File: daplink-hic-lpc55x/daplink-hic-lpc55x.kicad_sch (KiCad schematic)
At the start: 27 parts, among them J1 Conn_01x12_Socket, J2 Conn_01x12_Socket, SW2 SW_Push, U1 LPC55x16JEV98E, Y1 ABM8-16.000MHZ-B2-T

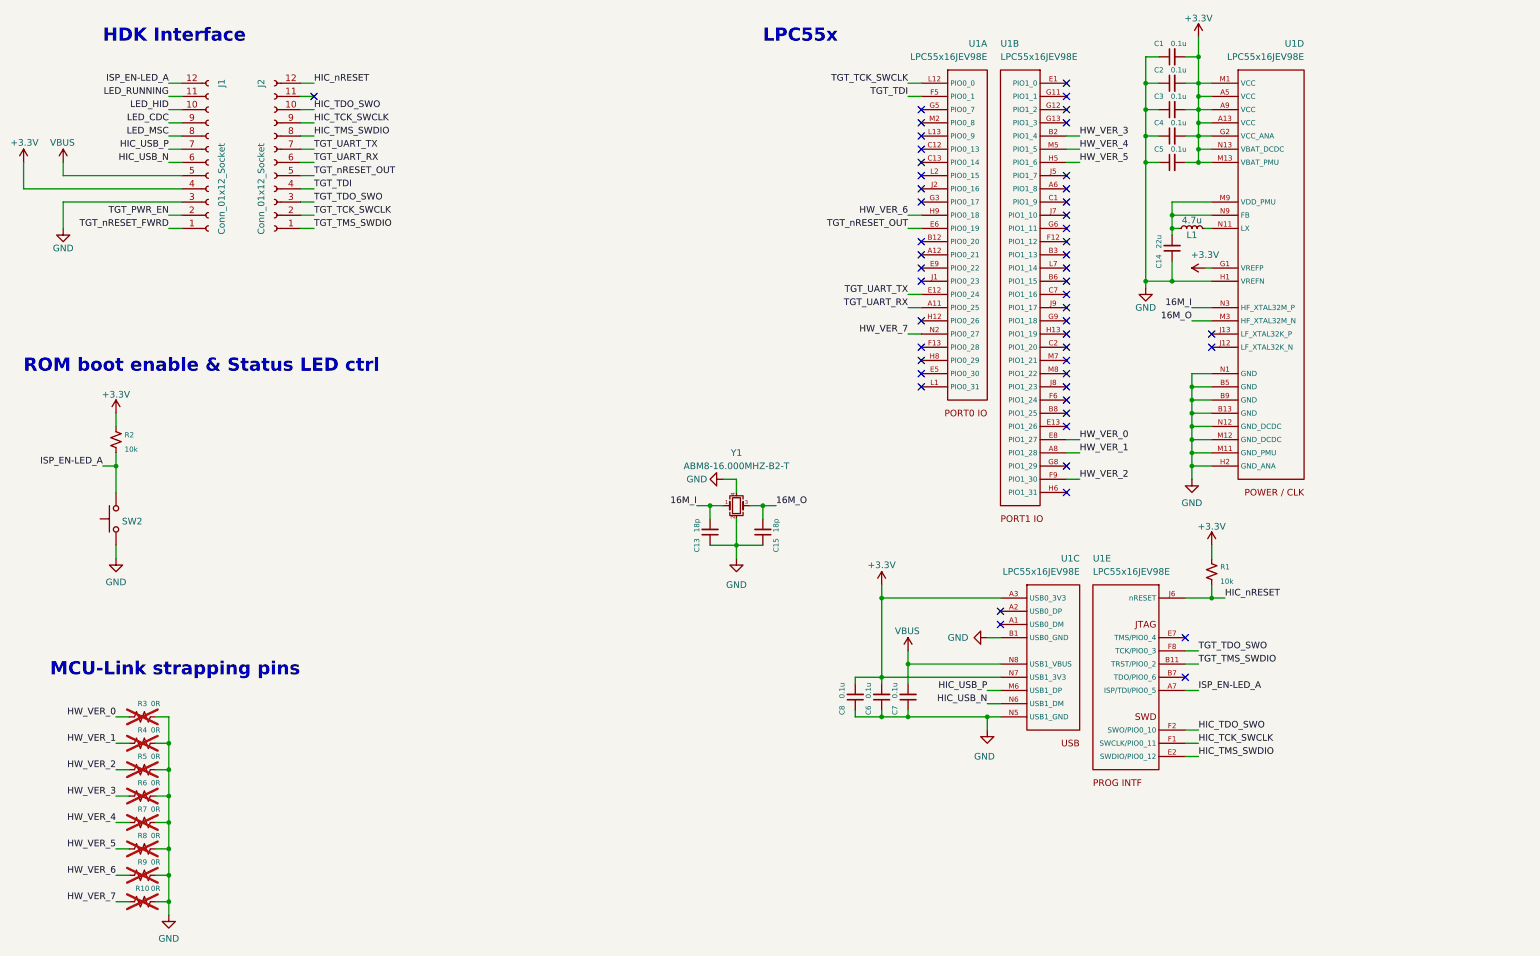
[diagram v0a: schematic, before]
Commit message: Update LPC package to the 100LQFP
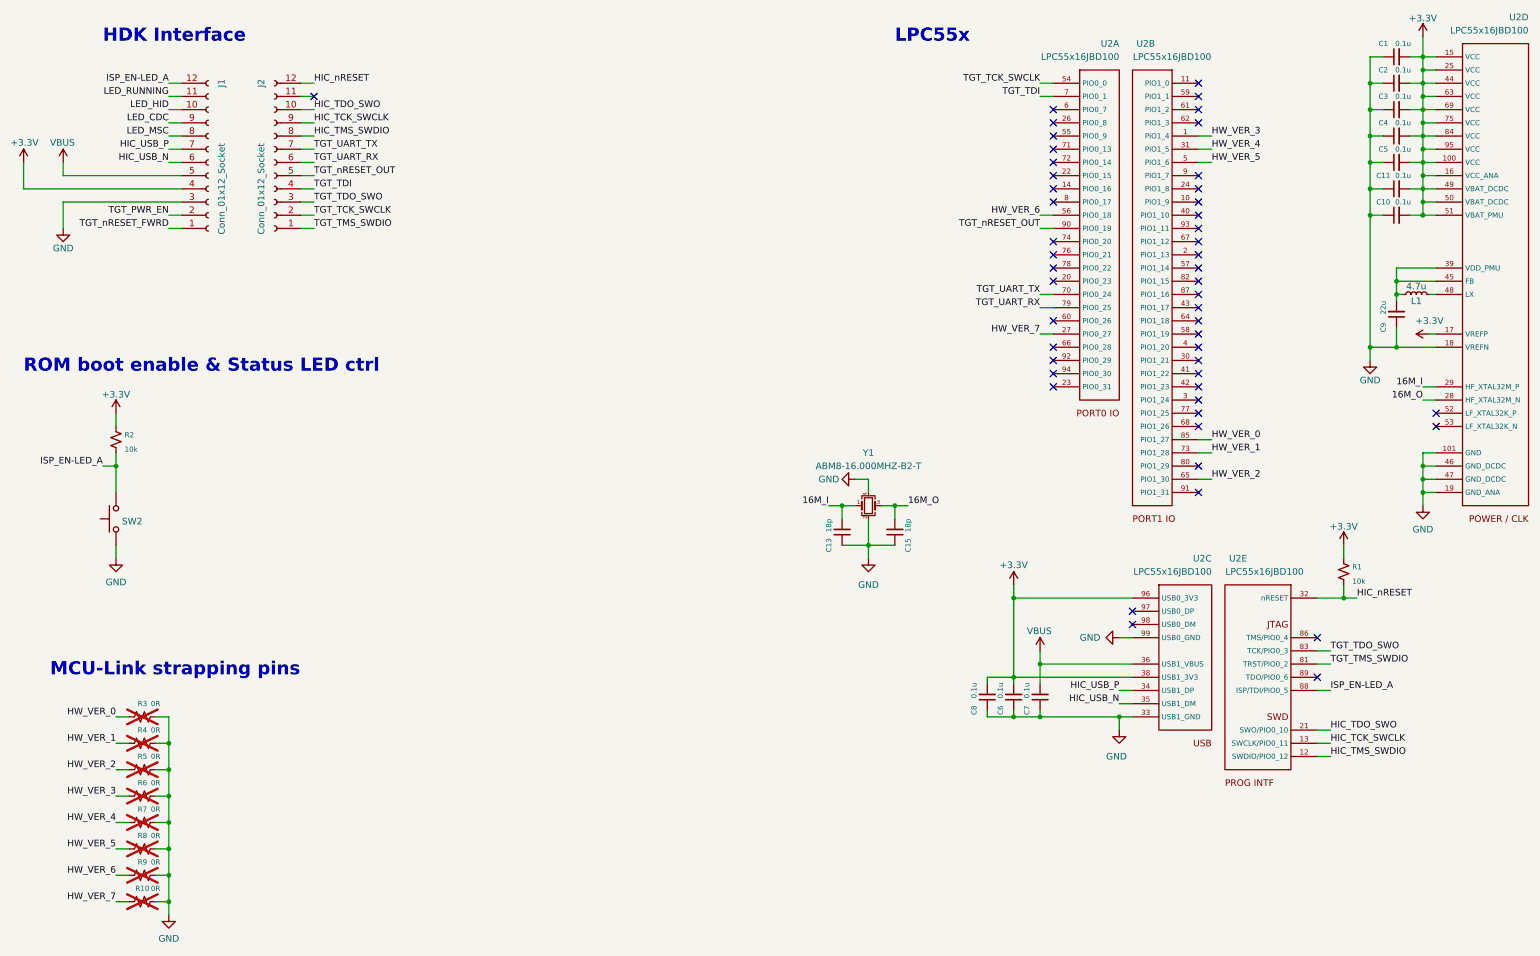
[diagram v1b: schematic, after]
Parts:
- removed C14: 22u, Capacitor_SMD:C_0603_1608Metric, symbol Device:C_Small
- removed U1: LPC55x16JEV98E, usb-dev:BGA-98_13x13_7.0x7.0mm, symbol usb-dev:LPC55x16JEV98E
- added C10, C11: 0.1u, Capacitor_SMD:C_0402_1005Metric, symbol Device:C_Small
- added C9: 22u, Capacitor_SMD:C_0603_1608Metric, symbol Device:C_Small
- added U2: LPC55x16JBD100, daplink-hic-lpc55x:QFP-100_14x14_Pitch0.5mm, symbol daplink-hic-lpc55x:LPC55x16JBD100
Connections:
- net +3V3: now also C10.2, C11.2, U2.100 (VCC), U2.15 (VCC), U2.16 (VCC_ANA), U2.17 (VREFP), U2.25 (VCC), U2.38 (USB1_3V3), U2.44 (VCC), U2.49 (VBAT_DCDC), U2.50 (VBAT_DCDC), U2.51 (VBAT_PMU), U2.63 (VCC), U2.69 (VCC), U2.75 (VCC), U2.84 (VCC), U2.95 (VCC), U2.96 (USB0_3V3)
- net 16M_I: now also U2.29 (HF_XTAL32M_P)
- net 16M_O: now also U2.28 (HF_XTAL32M_N)
- net GND: now also C10.1, C11.1, C9.1, U2.101 (GND), U2.18 (VREFN), U2.19 (GND_ANA), U2.33 (USB1_GND), U2.37 (USB1_GND), U2.46 (GND_DCDC), U2.47 (GND_DCDC), U2.99 (USB0_GND)
- net HIC_TCK_SWCLK: now also U2.13 (SWCLK/PIO0_11)
- net HIC_TDO_SWO: now also U2.21 (SWO/PIO0_10)
- net HIC_TMS_SWDIO: now also U2.12 (SWDIO/PIO0_12)
- net HIC_USB_N: now also U2.35 (USB1_DM)
- net HIC_USB_P: now also U2.34 (USB1_DP)
- net HIC_nRESET: now also U2.32 (nRESET)
- net HW_VER_0: now also U2.85 (PIO1_27)
- net HW_VER_1: now also U2.73 (PIO1_28)
- net HW_VER_2: now also U2.65 (PIO1_30)
- net HW_VER_3: now also U2.1 (PIO1_4)
- net HW_VER_4: now also U2.31 (PIO1_5)
- net HW_VER_5: now also U2.5 (PIO1_6)
- net HW_VER_6: now also U2.56 (PIO0_18)
- net HW_VER_7: now also U2.27 (PIO0_27)
- net ISP_EN-LED_A: now also U2.88 (ISP/TDI/PIO0_5)
- net TGT_TCK_SWCLK: now also U2.54 (PIO0_0)
- net TGT_TDI: now also U2.7 (PIO0_1)
- net TGT_TDO_SWO: now also U2.83 (TCK/PIO0_3)
- net TGT_TMS_SWDIO: now also U2.81 (TRST/PIO0_2)
- net TGT_UART_RX: now also U2.79 (PIO0_25)
- net TGT_UART_TX: now also U2.70 (PIO0_24)
- net TGT_nRESET_OUT: now also U2.90 (PIO0_19)
- net VBUS: now also U2.36 (USB1_VBUS)
- net at L1.1: now also C9.2, U2.39 (VDD_PMU), U2.45 (FB)
- net at L1.2: now also U2.48 (LX)
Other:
- moved on the sheet: C13, C15, C6, C7, C8, R1, Y1

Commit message: Add MPN info for the LPC55x
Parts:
- U2: MPN (none) -> LPC5516JBD100E; Manufacturer (none) -> NXP
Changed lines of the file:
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@@
+      (effects (font (size 1.27 1.27)) hide)
+    )
+    (property "Manufacturer" "NXP" (at 254 27.94 0)
+      (effects (font (size 1.27 1.27)) hide)
+    )
+    (property "MPN" "LPC5516JBD100E" (at 254 27.94 0)
       (effects (font (size 1.27 1.27)) hide)
     )
@@
       (effects (font (size 1.27 1.27)) hide)
     )
+    (property "Manufacturer" "NXP" (at 256.54 27.94 0)
+      (effects (font (size 1.27 1.27)) hide)
+    )
+    (property "MPN" "LPC5516JBD100E" (at 256.54 27.94 0)
+      (effects (font (size 1.27 1.27)) hide)
+    )
     (pin "14")
     (pin "20")
@@
       (effects (font (size 1.27 1.27)) hide)
     )
+    (property "Manufacturer" "NXP" (at 332.74 22.86 0)
+      (effects (font (size 1.27 1.27)) hide)
+    )
+    (property "MPN" "LPC5516JBD100E" (at 332.74 22.86 0)
+      (effects (font (size 1.27 1.27)) hide)
+    )
     (pin "14")
     (pin "20")
@@
       (effects (font (size 1.27 1.27)) hide)
     )
+    (property "MPN" "LPC5516JBD100E" (at 274.32 127 0)
+      (effects (font (size 1.27 1.27)) hide)
+    )
+    (property "Manufacturer" "NXP" (at 274.32 127 0)
+      (effects (font (size 1.27 1.27)) hide)
+    )
     (pin "14")
     (pin "20")
@@
       (effects (font (size 1.27 1.27)) hide)
     )
+    (property "Manufacturer" "NXP" (at 271.78 127 0)
+      (effects (font (size 1.27 1.27)) hide)
+    )
+    (property "MPN" "LPC5516JBD100E" (at 271.78 127 0)
+      (effects (font (size 1.27 1.27)) hide)
+    )
